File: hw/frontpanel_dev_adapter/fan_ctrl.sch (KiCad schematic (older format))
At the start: 9 parts, among them M401 Fan_4pin, Q401 DMG1012T, U401 74LVC2G17gw

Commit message: Frontpanel dev adapter: Optimize some LCSC components for JLC assembly; add some datasheets. Optimize F103 16MHz xtal routing
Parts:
- removed Q401: DMG1012T, customlib_mj_fp:SOT-523_handsoldering, symbol customlib_mj:DMG1012T
- added Q401: AO3400A, Package_TO_SOT_SMD:SOT-23, symbol Transistor_FET:AO3400A
- C402: footprint Capacitor_SMD:C_0603_1608Metric -> Capacitor_SMD:C_0402_1005Metric
- R401, R402, R403: footprint Resistor_SMD:R_0603_1608Metric -> Resistor_SMD:R_0402_1005Metric
- U401: footprint Package_TO_SOT_SMD:SOT-363_SC-70-6_Handsoldering -> Package_TO_SOT_SMD:SOT-363_SC-70-6
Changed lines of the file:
@@
 F 0 "U401" H 3225 3883 50  0000 C CNN
 F 1 "74LVC2G17gw" H 3225 3974 50  0000 C CNN
-F 2 "Package_TO_SOT_SMD:SOT-363_SC-70-6_Handsoldering" H 3250 4150 50  0001 C CNN
+F 2 "Package_TO_SOT_SMD:SOT-363_SC-70-6" H 3250 4150 50  0001 C CNN
 F 3 "http://www.ti.com/lit/sg/scyt129e/scyt129e.pdf" H 3250 4150 50  0001 C CNN
 	1    3250 4150
@@
 F 0 "R403" H 4450 4750 50  0000 L CNN
 F 1 "10k" H 4450 4850 50  0000 L CNN
-F 2 "Resistor_SMD:R_0603_1608Metric" H 4400 4800 50  0001 C CNN
+F 2 "Resistor_SMD:R_0402_1005Metric" H 4400 4800 50  0001 C CNN
 F 3 "~" H 4400 4800 50  0001 C CNN
 	1    4400 4800
 	-1   0    0    1
-$EndComp
-$Comp
-L customlib_mj:DMG1012T Q?
-U 1 1 5F473D01
-P 4700 4650
-AR Path="/5F472FC2/5F4722BA/5F473D01" Ref="Q?"  Part="1"
-AR Path="/5F472FC2/5F472468/5F473D01" Ref="Q?"  Part="1"
-AR Path="/5F472FC2/5F472567/5F473D01" Ref="Q?"  Part="1"
-AR Path="/5FD9592B/5F4722BA/5F473D01" Ref="Q?"  Part="1"
-AR Path="/5FD9592B/5FDAF153/5F473D01" Ref="Q401"  Part="1"
-F 0 "Q401" H 4906 4696 50  0000 L CNN
-F 1 "DMG1012T" H 5102 4605 50  0000 C CNN
-F 2 "customlib_mj_fp:SOT-523_handsoldering" H 4900 4750 50  0001 C CNN
-F 3 "https://www.diodes.com/assets/Datasheets/ds31783.pdf" H 4700 4650 50  0001 C CNN
-	1    4700 4650
-	1    0    0    -1
 $EndComp
 $Comp
@@
 F 0 "R401" V 4900 3800 50  0000 C CNN
 F 1 "12k" V 4700 3800 50  0000 C CNN
-F 2 "Resistor_SMD:R_0603_1608Metric" H 4800 3800 50  0001 C CNN
+F 2 "Resistor_SMD:R_0402_1005Metric" H 4800 3800 50  0001 C CNN
 F 3 "~" H 4800 3800 50  0001 C CNN
 	1    4800 3800
@@
 F 0 "R402" H 3850 4500 50  0000 L CNN
 F 1 "10k" H 3850 4600 50  0000 L CNN
-F 2 "Resistor_SMD:R_0603_1608Metric" H 3800 4550 50  0001 C CNN
+F 2 "Resistor_SMD:R_0402_1005Metric" H 3800 4550 50  0001 C CNN
 F 3 "~" H 3800 4550 50  0001 C CNN
 	1    3800 4550
@@
 F 0 "U401" H 3266 5196 50  0000 C CNN
 F 1 "74LVC2G17gw" H 3266 5105 50  0000 C CNN
-F 2 "Package_TO_SOT_SMD:SOT-363_SC-70-6_Handsoldering" H 3000 5150 50  0001 C CNN
+F 2 "Package_TO_SOT_SMD:SOT-363_SC-70-6" H 3000 5150 50  0001 C CNN
 F 3 "http://www.ti.com/lit/sg/scyt129e/scyt129e.pdf" H 3000 5150 50  0001 C CNN
 	3    3000 5150
@@
 F 0 "C402" H 2550 5050 50  0000 L CNN
 F 1 "100n" H 2550 5250 50  0000 L CNN
-F 2 "Capacitor_SMD:C_0603_1608Metric" H 2500 5150 50  0001 C CNN
+F 2 "Capacitor_SMD:C_0402_1005Metric" H 2500 5150 50  0001 C CNN
 F 3 "~" H 2500 5150 50  0001 C CNN
 	1    2500 5150
@@
 F 0 "U401" H 3125 6133 50  0000 C CNN
 F 1 "74LVC2G17gw" H 3125 6224 50  0000 C CNN
-F 2 "Package_TO_SOT_SMD:SOT-363_SC-70-6_Handsoldering" H 3150 6400 50  0001 C CNN
+F 2 "Package_TO_SOT_SMD:SOT-363_SC-70-6" H 3150 6400 50  0001 C CNN
 F 3 "http://www.ti.com/lit/sg/scyt129e/scyt129e.pdf" H 3150 6400 50  0001 C CNN
 	2    3150 6400
@@
 	3600 6400 3450 6400
 NoConn ~ 2900 6400
+$Comp
+L Transistor_FET:AO3400A Q401
+U 1 1 6034804E
+P 4700 4650
+F 0 "Q401" H 4905 4696 50  0000 L CNN
+F 1 "AO3400A" H 4905 4605 50  0000 L CNN
+F 2 "Package_TO_SOT_SMD:SOT-23" H 4900 4575 50  0001 L CIN
+F 3 "http://www.aosmd.com/pdfs/datasheet/AO3400A.pdf" H 4700 4650 50  0001 L CNN
+	1    4700 4650
+	1    0    0    -1
+$EndComp
 $EndSCHEMATC

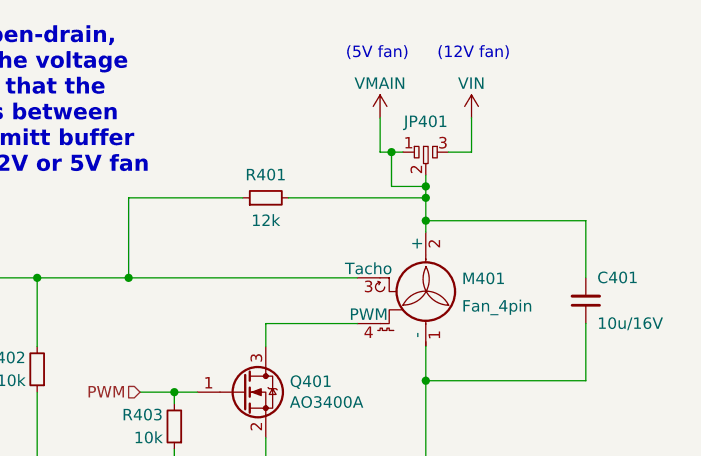
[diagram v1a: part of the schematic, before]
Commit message: FP adapter/dev board: *routing DONE* ; minor pinout tweaks (optimize routing); fix some missing 3d models
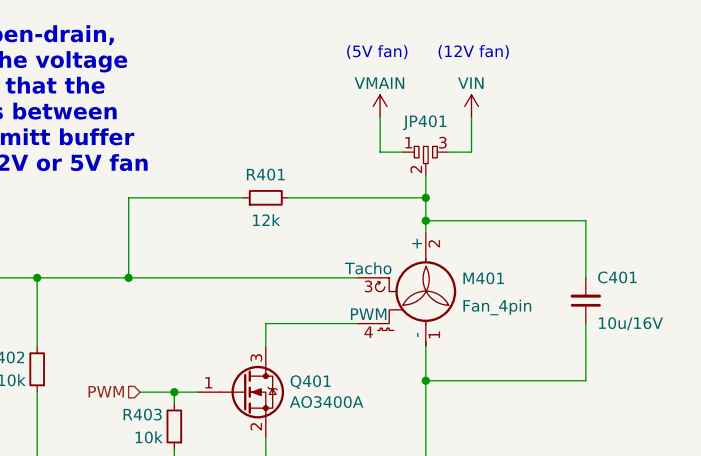
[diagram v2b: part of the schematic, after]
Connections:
- net VMAIN: no longer C401.2, JP401.2, M401.2 (+), R401.2
- new net: C401.2, JP401.2, M401.2 (+), R401.2
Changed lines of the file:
@@
 	1    0    0    -1
 $EndComp
-Wire Wire Line
-	5500 3700 5500 3750
 $Comp
 L power:GND #PWR?
@@
 Wire Wire Line
 	5300 3450 5300 3600
-Wire Wire Line
-	5300 3600 5350 3600
 Wire Wire Line
 	5700 3450 5700 3600
@@
 Text Notes 2450 3700 0    70   ~ 14
 Fan pin3 (Tacho) is open-drain,\n2 pulses/revolution. The voltage\ndivider should ensure that the\ninactive (high) level is between\n2.2 .. 5.5V for the Schmitt buffer\ninput, regardless of 12V or 5V fan
-Wire Wire Line
-	5350 3750 5500 3750
-Wire Wire Line
-	5350 3600 5350 3750
-Connection ~ 5350 3600
-Wire Wire Line
-	5350 3600 5400 3600
-Connection ~ 5500 3750
-Wire Wire Line
-	5500 3750 5500 3800
 $Comp
 L customlib_mj:dogbone_3_ud JP?
@@
 	1    0    0    -1
 $EndComp
+Wire Wire Line
+	5500 3700 5500 3800
+Wire Wire Line
+	5300 3600 5400 3600
 $EndSCHEMATC

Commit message: FP adapter board: Added LCSC partnumbers to all components to be PnP:ed; Finalized some silk additions; Generated Gerbers, BoM & pnp-files for JCL assembly
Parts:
- C401: footprint Capacitor_SMD:C_0603_1608Metric -> Capacitor_SMD:C_0805_2012Metric; LCSC (none) -> C15850
- C402: LCSC (none) -> C1525
- Q401: LCSC (none) -> C20917
- R401: LCSC (none) -> C25752
- R402, R403: LCSC (none) -> C25744
- U401: LCSC (DNM) (none) -> C80500
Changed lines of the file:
@@
 F 2 "Package_TO_SOT_SMD:SOT-363_SC-70-6" H 3250 4150 50  0001 C CNN
 F 3 "http://www.ti.com/lit/sg/scyt129e/scyt129e.pdf" H 3250 4150 50  0001 C CNN
+F 4 "C80500" H 3250 4150 50  0001 C CNN "LCSC (DNM)"
 	1    3250 4150
 	-1   0    0    1
@@
 F 2 "Resistor_SMD:R_0402_1005Metric" H 4400 4800 50  0001 C CNN
 F 3 "~" H 4400 4800 50  0001 C CNN
+F 4 "C25744" H 4400 4800 50  0001 C CNN "LCSC"
 	1    4400 4800
 	-1   0    0    1
@@
 F 2 "Resistor_SMD:R_0402_1005Metric" H 4800 3800 50  0001 C CNN
 F 3 "~" H 4800 3800 50  0001 C CNN
+F 4 "C25752" V 4800 3800 50  0001 C CNN "LCSC"
 	1    4800 3800
 	0    -1   -1   0
@@
 F 2 "Resistor_SMD:R_0402_1005Metric" H 3800 4550 50  0001 C CNN
 F 3 "~" H 3800 4550 50  0001 C CNN
+F 4 "C25744" H 3800 4550 50  0001 C CNN "LCSC"
 	1    3800 4550
 	-1   0    0    1
@@
 F 2 "Package_TO_SOT_SMD:SOT-363_SC-70-6" H 3000 5150 50  0001 C CNN
 F 3 "http://www.ti.com/lit/sg/scyt129e/scyt129e.pdf" H 3000 5150 50  0001 C CNN
+F 4 "C80500" H 3000 5150 50  0001 C CNN "LCSC (DNM)"
 	3    3000 5150
 	1    0    0    -1
@@
 F 2 "Capacitor_SMD:C_0402_1005Metric" H 2500 5150 50  0001 C CNN
 F 3 "~" H 2500 5150 50  0001 C CNN
+F 4 "C1525" H 2500 5150 50  0001 C CNN "LCSC"
 	1    2500 5150
 	1    0    0    1
@@
 F 0 "C401" H 6250 4150 50  0000 L CNN
 F 1 "10u/16V" H 6250 4350 50  0000 L CNN
-F 2 "Capacitor_SMD:C_0603_1608Metric" H 6200 4250 50  0001 C CNN
+F 2 "Capacitor_SMD:C_0805_2012Metric" H 6200 4250 50  0001 C CNN
 F 3 "~" H 6200 4250 50  0001 C CNN
+F 4 "C15850" H 6200 4250 50  0001 C CNN "LCSC"
 	1    6200 4250
 	1    0    0    1
@@
 F 2 "Package_TO_SOT_SMD:SOT-363_SC-70-6" H 3150 6400 50  0001 C CNN
 F 3 "http://www.ti.com/lit/sg/scyt129e/scyt129e.pdf" H 3150 6400 50  0001 C CNN
+F 4 "C80500" H 3150 6400 50  0001 C CNN "LCSC (DNM)"
 	2    3150 6400
 	-1   0    0    1
@@
 F 2 "Package_TO_SOT_SMD:SOT-23" H 4900 4575 50  0001 L CIN
 F 3 "http://www.aosmd.com/pdfs/datasheet/AO3400A.pdf" H 4700 4650 50  0001 L CNN
+F 4 "C20917" H 4700 4650 50  0001 C CNN "LCSC"
 	1    4700 4650
 	1    0    0    -1

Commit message: * Some uncomitted frontpanel devboard (R1A) files * Some files frontpanel devboard files updated (not sure what changed, except fan-header from customlib_mj)
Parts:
- M401: symbol Motor:Fan_4pin -> customlib_mj:Fan_4pin
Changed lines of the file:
@@
 $EndComp
 $Comp
-L Motor:Fan_4pin M?
+L customlib_mj:Fan_4pin M?
 U 1 1 5F47830A
 P 5500 4250
